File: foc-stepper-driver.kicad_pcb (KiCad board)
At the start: 4 copper layers, 42 x 42 mm, 72 parts, among them CN1 C42391660, CN2 C2839706, CN3 C2839705, CN4 C2839704, J2 TC2030, U1 DRV8962DDWR, U2 TYPE-C 16PLT-H10.0, U3 STM32G431CBT6, U6 AS5047P-ATSM, U7 TPS560430XDBVR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

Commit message: update
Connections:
- U1 pad 45: unconnected-(U1-EP-Pad45) -> GND
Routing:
- net GND: track 61.1 -> 66.2 mm, vias 62 -> 70
- added copper zone on F.Cu, net GND
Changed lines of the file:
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@@
 	(net 79 "/STM32G431CBT6/USBC_CONN_D-")
 	(net 80 "unconnected-(J2-Pad3)")
-	(net 81 "unconnected-(U1-EP-Pad45)")
 	(footprint "Capacitor_SMD:C_0402_1005Metric"
 		(layer "F.Cu")
@@
 			(size 3.9 8)
 			(layers "F.Cu" "F.Mask" "F.Paste")
-			(net 81 "unconnected-(U1-EP-Pad45)")
+			(net 1 "GND")
 			(pinfunction "EP")
-			(pintype "unspecified+no_connect")
+			(pintype "unspecified")
 		)
 		(embedded_fonts no)
@@
 	)
 	(segment
+		(start 145.477834 83.135166)
+		(end 145.05 83.563)
+		(width 0.5)
+		(layer "F.Cu")
+		(net 1)
+	)
+	(segment
 		(start 137.14 77.51)
 		(end 137.15 77.5)
@@
 	)
 	(segment
+		(start 147.460162 83.135166)
+		(end 145.477834 83.135166)
+		(width 0.5)
+		(layer "F.Cu")
+		(net 1)
+	)
+	(segment
 		(start 129.169 77.3)
 		(end 129.92 77.3)
@@
 	)
 	(segment
+		(start 147.458012 83.978553)
+		(end 145.465553 83.978553)
+		(width 0.5)
+		(layer "F.Cu")
+		(net 1)
+	)
+	(segment
 		(start 118.8875 87.860034)
 		(end 120.269966 87.860034)
@@
 	)
 	(segment
+		(start 145.465553 83.978553)
+		(end 145.05 83.563)
+		(width 0.5)
+		(layer "F.Cu")
+		(net 1)
+	)
+	(segment
 		(start 120.269966 87.860034)
 		(end 120.27 87.86)
@@
 	)
 	(via
+		(at 147.38 81.45)
+		(size 0.7)
+		(drill 0.3)
+		(layers "F.Cu" "B.Cu")
+		(free yes)
+		(net 1)
+	)
+	(via
 		(at 131.939635 81.413191)
 		(size 0.4)
@@
 	)
 	(via
+		(at 142.78 83.24)
+		(size 0.4)
+		(drill 0.15)
+		(layers "F.Cu" "B.Cu")
+		(free yes)
+		(net 1)
+	)
+	(via
 		(at 133.705644 92.119356)
 		(size 0.4)
@@
 	)
 	(via
+		(at 147.38 80.5)
+		(size 0.7)
+		(drill 0.3)
+		(layers "F.Cu" "B.Cu")
+		(free yes)
+		(net 1)
+	)
+	(via
 		(at 124.73 68.17)
 		(size 0.4)
@@
 	)
 	(via
+		(at 147.38 86.71)
+		(size 0.7)
+		(drill 0.3)
+		(layers "F.Cu" "B.Cu")
+		(free yes)
+		(net 1)
+	)
+	(via
 		(at 116.43 83.07)
 		(size 0.5)
@@
 	)
 	(via
+		(at 147.38 82.42)
+		(size 0.7)
+		(drill 0.3)
+		(layers "F.Cu" "B.Cu")
+		(free yes)
+		(net 1)
+	)
+	(via
+		(at 147.38 84.79)
+		(size 0.7)
+		(drill 0.3)
+		(layers "F.Cu" "B.Cu")
+		(free yes)
+		(net 1)
+	)
+	(via
 		(at 147.458012 83.978553)
 		(size 0.6)
@@
 	)
 	(via
+		(at 147.38 85.75)
+		(size 0.7)
+		(drill 0.3)
+		(layers "F.Cu" "B.Cu")
+		(free yes)
+		(net 1)
+	)
+	(via
 		(at 129.1 93.62)
 		(size 0.4)
@@
 	)
 	(via
+		(at 142.76 80.7)
+		(size 0.4)
+		(drill 0.15)
+		(layers "F.Cu" "B.Cu")
+		(free yes)
+		(net 1)
+	)
+	(via
 		(at 120.27 87.86)
 		(size 0.4)
@@
 	)
 	(segment
-		(start 135.31 82.45)
-		(end 135.310876 82.449124)
-		(width 0.29)
+		(start 147.525168 83.135166)
+		(end 147.540002 83.15)
+		(width 0.5)
 		(layer "B.Cu")
 		(net 1)
 	)
 	(segment
-		(start 148.21 83.15)
-		(end 148.27 83.09)
-		(width 0.5)
+		(start 135.31 82.45)
+		(end 135.310876 82.449124)
+		(width 0.29)
 		(layer "B.Cu")
 		(net 1)
 	)
 	(segment
-		(start 147.460162 83.135166)
-		(end 147.525168 83.135166)
+		(start 131.233095 80.246902)
+		(end 130.466902 80.246902)
 		(width 0.5)
 		(layer "B.Cu")
@@
 	)
 	(segment
-		(start 147.458012 83.978553)
-		(end 147.501447 83.978553)
+		(start 138.62 89.17)
+		(end 137.63 89.17)
 		(width 0.5)
 		(layer "B.Cu")
@@
 	)
 	(segment
-		(start 131.233095 80.246902)
-		(end 130.466902 80.246902)
+		(start 147.501447 83.978553)
+		(end 147.51 83.97)
 		(width 0.5)
 		(layer "B.Cu")
@@
 	)
 	(segment
-		(start 138.62 89.17)
-		(end 137.63 89.17)
+		(start 147.540002 83.15)
+		(end 148.21 83.15)
 		(width 0.5)
 		(layer "B.Cu")
@@
 	)
 	(segment
-		(start 137.7 92.32)
-		(end 137.67 92.29)
+		(start 147.458012 83.978553)
+		(end 147.501447 83.978553)
 		(width 0.5)
 		(layer "B.Cu")
@@
 	)
 	(segment
-		(start 137.63 89.17)
-		(end 137.62 89.18)
+		(start 148.21 83.15)
+		(end 148.27 83.09)
 		(width 0.5)
 		(layer "B.Cu")
@@
 	)
 	(segment
-		(start 147.501447 83.978553)
-		(end 147.51 83.97)
+		(start 137.7 92.32)
+		(end 137.67 92.29)
 		(width 0.5)
 		(layer "B.Cu")
@@
 	)
 	(segment
-		(start 147.540002 83.15)
-		(end 148.21 83.15)
+		(start 147.51 83.97)
+		(end 148.23 83.97)
 		(width 0.5)
 		(layer "B.Cu")
@@
 	)
 	(segment
-		(start 147.525168 83.135166)
-		(end 147.540002 83.15)
+		(start 137.63 89.17)
+		(end 137.62 89.18)
 		(width 0.5)
 		(layer "B.Cu")
@@
 	)
 	(segment
+		(start 147.460162 83.135166)
+		(end 147.525168 83.135166)
+		(width 0.5)
+		(layer "B.Cu")
+		(net 1)
+	)
+	(segment
 		(start 130.466902 80.246902)
 		(end 130.46 80.24)
@@
 	)
 	(segment
-		(start 147.51 83.97)
-		(end 148.23 83.97)
-		(width 0.5)
-		(layer "B.Cu")
-		(net 1)
-	)
-	(segment
 		(start 132.42 90.279774)
 		(end 131.594774 91.105)
@@
 			)
 		)
+	)
+	(zone
+		(net 1)
+		(net_name "GND")
+		(layer "F.Cu")
+		(hatch edge 0.5)
+		(priority 35)
+		(connect_pads yes
+			(clearance 0.3)
+		)
+		(min_thickness 0.25)
+		(filled_areas_thickness no)
+		(fill yes
+			(thermal_gap 0.5)
+			(thermal_bridge_width 0.5)
+		)
+		(polygon
+			(pts
+				(xy 142.96 79.4) (xy 142.96 87.71) (xy 147.16 87.71) (xy 147.83 87.04) (xy 147.83 80.17) (xy 147.06 79.4)
+			)
+		)

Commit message: update
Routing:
- net +24V: track 11.1 -> 22.1 mm, vias 2 -> 10
- net GND: track 66.2 -> 66.6 mm, vias 70 -> 68

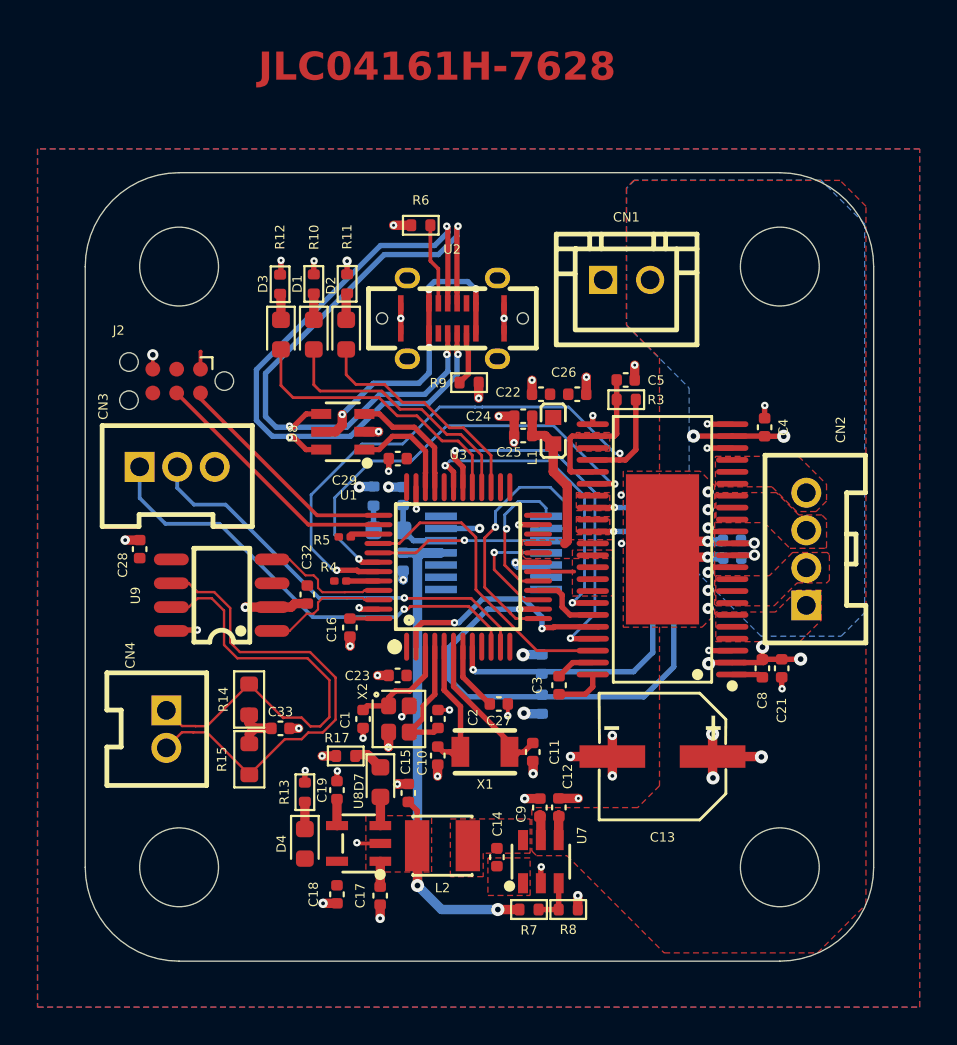
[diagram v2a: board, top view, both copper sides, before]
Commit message: update trace width
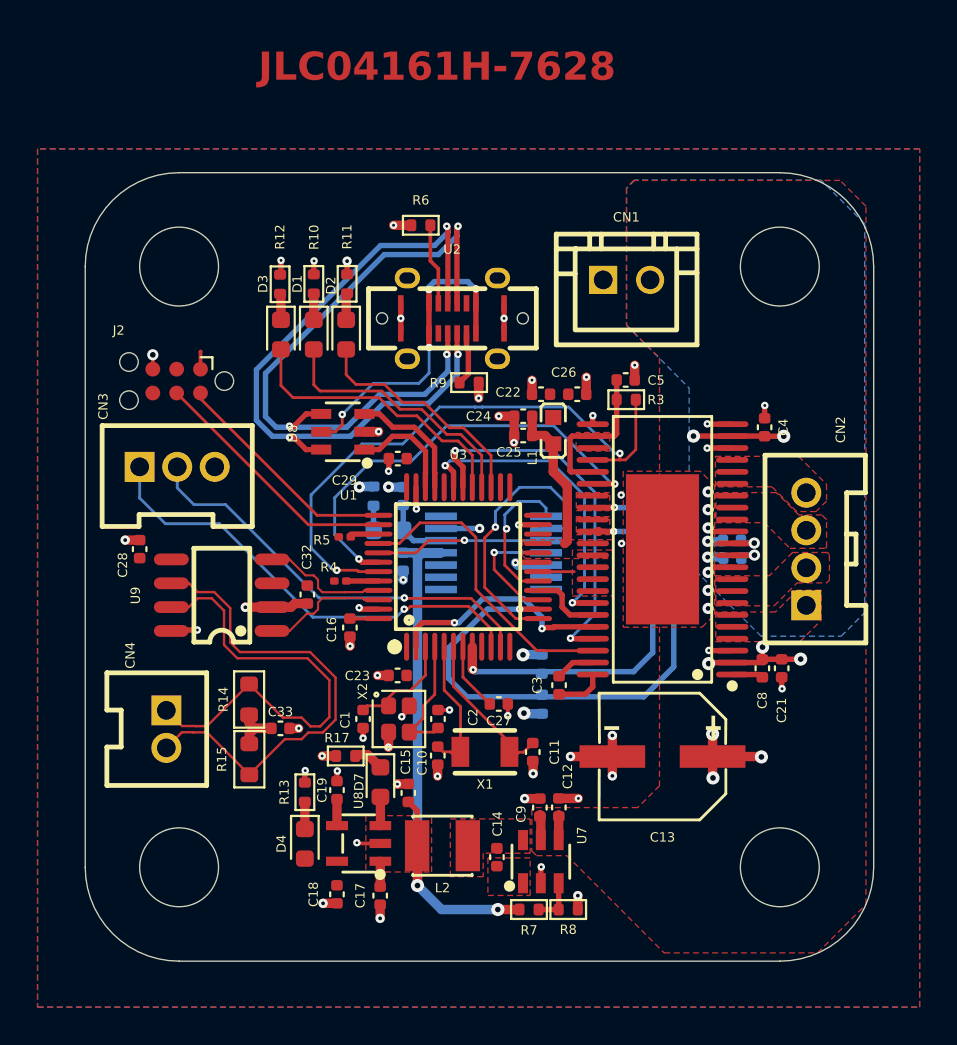
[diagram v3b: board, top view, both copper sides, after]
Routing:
- net GND: track 66.6 -> 62.6 mm

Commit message: update
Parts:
- R14, R15: value 60 -> 60.4; footprint PCM_Resistor_SMD_AKL:R_0603_1608Metric -> PCM_Resistor_SMD_AKL:R_0402_1005Metric
- moved R17 9.13 mm to (130.6, 103.4), turned to 0 degrees
- moved R13 7.08 mm to (124.4, 103.4), turned to 180 degrees
- moved D7 6.73 mm to (128.6, 102.5), turned to 90 degrees
- moved C32 5.68 mm to (121.6, 82.6), turned to 180 degrees
- moved C18 3.79 mm to (124.9, 99.4), turned to -90 degrees
- moved C22 3.65 mm to (137.5, 78.8)
- moved D4 3.33 mm to (126.2, 102.6), turned to 90 degrees
- moved C17 2.56 mm to (130.1, 99.5), turned to -90 degrees
- moved C15 1.75 mm to (130.1, 97.5)
- moved U8 1.44 mm to (127.5, 98.9)
- moved C19 1.42 mm to (126.3, 96.2)
- moved C23 1.19 mm to (129.8, 90.3)
- moved C16 1.11 mm to (128.4, 88.8)
- moved J2 1.05 mm to (119.2, 73.5)
- moved CN3 0.92 mm to (119.2, 78.2)
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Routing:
- net +3.3V: track 2.48 -> 30.8 mm, vias 0 -> 12
- net /STM32G431CBT6/USBC_CONN_D-: track 35.5 -> 15.8 mm, vias 3 -> 2
- net /STM32G431CBT6/USBC_CONN_D+: track 37.1 -> 19.8 mm
- net +24V: track 22.1 -> 29.8 mm
- net +5V: track 34.4 -> 31.1 mm
- net /DRV8962DDWR/DRV8962_IPROPI1: track 20.2 -> 17.1 mm
- net /DRV8962DDWR/DRV8962_IPROPI3: track 31.9 -> 29.8 mm
- net /DRV8962DDWR/DRV8962_nFAULT: track 31.9 -> 33.9 mm
- net GND: track 62.6 -> 61.1 mm, vias 68 -> 54
- net Net-(C33-Pad1): track 3.64 -> 2.46 mm
- net /STM32G431CBT6/STM32_SWCLK: track 13.7 -> 14.8 mm
- net Net-(D8-Pad5): track 17.1 -> 18.1 mm
- net /STM32G431CBT6/STM32_SWDIO: track 12.4 -> 13.2 mm
- net /STM32G431CBT6/STM32_USART_TX: track 24.7 -> 25.4 mm
- net /AS5047P/AS5047P_SPI_CSn: track 7.96 -> 8.61 mm
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- added copper zone on In2.Cu, net +3.3V
- removed copper zone on In2.Cu, net GND

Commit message: update
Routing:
- net GND: track 61.1 -> 62.8 mm, vias 54 -> 56
- net /DRV8962DDWR/DRV8962_nFAULT: track 33.9 -> 34.6 mm

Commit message: update
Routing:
- net GND: track 62.8 -> 63.1 mm, vias 56 -> 59

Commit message: update
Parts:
- moved C30 0.28 mm to (131.0, 84.2)
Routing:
- net /DRV8962DDWR/DRV8962_EN: track 1.93 -> 0.00 mm
- net +3.3V: track 30.8 -> 29.6 mm
- removed copper zone on F.Cu, net +3.3V
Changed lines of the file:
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@@
 	(footprint "Capacitor_SMD:C_0402_1005Metric"
 		(layer "B.Cu")
-		(at 131.233095 84.225 -90)
+		(at 130.96 84.19 -90)
 		(descr "Capacitor SMD 0402 (1005 Metric), square (rectangular) end terminal, IPC-7351 nominal, (Body size source: IPC-SM-782 page 76, https://www.pcb-3d.com/wordpress/wp-content/uploads/ipc-sm-782a_amendment_1_and_2.pdf), generated with kicad-footprint-generator")
 		(tags "capacitor")
@@
 	)
 	(segment
-		(start 147.592678 88.9605)
-		(end 147.532452 88.900274)
-		(width 0.29)
-		(layer "F.Cu")
-		(net 1)
-	)
-	(segment
 		(start 137.15 77.34)
 		(end 136.485 77.34)
@@
 	)
 	(segment
+		(start 147.720489 88.9605)
+		(end 148.7645 88.9605)
+		(width 0.29)
+		(layer "F.Cu")
+		(net 1)
+	)
+	(segment
 		(start 128.47 90.28)
 		(end 128.46 90.27)
@@
 	)
 	(segment
-		(start 148.7645 88.9605)
-		(end 147.592678 88.9605)
-		(width 0.29)
-		(layer "F.Cu")
-		(net 1)
-	)
-	(segment
 		(start 139.53 96.83)
 		(end 140.57 96.83)
@@
 		(net 1)
 	)
+	(segment
+		(start 147.679439 88.91945)
+		(end 147.720489 88.9605)
+		(width 0.29)
+		(layer "F.Cu")
+		(net 1)
+	)
 	(via
 		(at 132.32 103.35)
@@
 	)
 	(via
-		(at 147.43 78.17)
+		(at 131.247313 85.40185)
 		(size 0.6)
 		(drill 0.3)
@@
 	)
 	(via
-		(at 141.34 76.44)
+		(at 147.43 78.17)
 		(size 0.6)
 		(drill 0.3)
@@
 	)
 	(via
-		(at 137.71 96.84)
+		(at 141.34 76.44)
 		(size 0.6)
 		(drill 0.3)
@@
 	)
 	(via
-		(at 131.24 85.19)
+		(at 137.71 96.84)
 		(size 0.6)
 		(drill 0.3)
@@
 	)
 	(via
-		(at 147.532452 88.900274)
+		(at 147.679439 88.91945)
 		(size 0.6)
 		(drill 0.3)
@@
 	)
 	(segment
-		(start 148.27 83.09)
-		(end 147.4 83.09)
+		(start 131.233095 85.387632)
+		(end 131.247313 85.40185)
 		(width 0.29)
 		(layer "B.Cu")
@@
 	)
 	(segment
-		(start 131.233095 80.246902)
-		(end 130.466902 80.246902)
-		(width 0.5)
+		(start 148.27 83.09)
+		(end 147.4 83.09)
+		(width 0.29)
 		(layer "B.Cu")
 		(net 1)
 	)
 	(segment
-		(start 131.233095 85.183095)
-		(end 131.24 85.19)
+		(start 131.233095 80.246902)
+		(end 130.466902 80.246902)
 		(width 0.5)
 		(layer "B.Cu")
@@
 	)
 	(segment
+		(start 131.233095 84.943095)
+		(end 131.233095 85.387632)
+		(width 0.29)
+		(layer "B.Cu")
+		(net 1)
+	)
+	(segment
 		(start 138.85 84.4)
 		(end 137.345 84.4)
@@
 	)
 	(segment
-		(start 131.233095 84.705)
-		(end 131.233095 85.183095)
-		(width 0.5)
+		(start 130.96 84.67)
+		(end 131.233095 84.943095)
+		(width 0.29)
 		(layer "B.Cu")
 		(net 1)
@@
 	)
 	(segment
-		(start 132.8 102.75)
-		(end 136.28 102.75)
+		(start 133.25 83.75)
+		(end 131.238095 83.75)
 		(width 0.5)
 		(layer "B.Cu")
@@
 	)
 	(segment
-		(start 132 101.47)
-		(end 132 83.99)
+		(start 132.8 102.75)
+		(end 136.28 102.75)
 		(width 0.5)
 		(layer "B.Cu")
@@
 	)
 	(segment
-		(start 131.238095 83.75)
-		(end 131.233095 83.745)
+		(start 131.198095 83.71)
+		(end 130.96 83.71)
 		(width 0.5)
 		(layer "B.Cu")
@@
 	)
 	(segment
-		(start 133.25 83.75)
-		(end 131.238095 83.75)
+		(start 132 101.47)
+		(end 132 83.99)
 		(width 0.5)
 		(layer "B.Cu")
@@
 	)
 	(segment
+		(start 131.238095 83.75)
+		(end 131.198095 83.71)
+		(width 0.5)
+		(layer "B.Cu")
+		(net 11)
+	)
+	(segment
 		(start 120.44 73.09)
 		(end 120.425 73.075)
@@
 	)
 	(segment
-		(start 140.03 74.355)
-		(end 140.025 74.35)
-		(width 0.29)
-		(layer "F.Cu")
-		(net 12)
-	)
-	(segment
 		(start 137.96 78.15)
 		(end 137.95 78.14)
@@
 	)
 	(segment
-		(start 139.06 75.3)
-		(end 139.06 74.335)
-		(width 0.29)
-		(layer "F.Cu")
-		(net 12)
-	)
-	(segment
 		(start 117.270034 84.100034)
 		(end 117.2 84.03)
@@
 	)
 	(segment
+		(start 140.03 75.3)
+		(end 140.03 74.44)
+		(width 0.5)
+		(layer "F.Cu")
+		(net 12)
+	)
+	(segment
 		(start 122.055 82.575)
 		(end 123 82.575)
@@
 	)
 	(segment
-		(start 139.06 75.3)
-		(end 140.03 75.3)
+		(start 127.083805 82.9)
+		(end 127.074821 82.891016)
+		(width 0.5)
+		(layer "F.Cu")
+		(net 12)
+	)
+	(segment
+		(start 137.96 78.78)
+		(end 138.42 79.24)
 		(width 0.29)
 		(layer "F.Cu")
@@
 	)
 	(segment
-		(start 127.083805 82.9)
-		(end 127.074821 82.891016)
+		(start 139.23 76.54)
+		(end 139.23 75.675)
 		(width 0.5)
 		(layer "F.Cu")
@@
 	)
 	(segment
-		(start 120.44 71.76)
-		(end 120.45 71.75)
-		(width 0.5)
+		(start 138.42 79.24)
+		(end 138.42 81.75)
+		(width 0.29)
 		(layer "F.Cu")
 		(net 12)
 	)
 	(segment
-		(start 139.06 74.335)
-		(end 139.05 74.325)
-		(width 0.29)
+		(start 120.44 71.76)
+		(end 120.45 71.75)
+		(width 0.5)
 		(layer "F.Cu")
 		(net 12)
 	)
 	(segment
-		(start 138.08 78.78)
-		(end 137.96 78.78)
-		(width 0.15)
+		(start 139.23 75.675)
+		(end 139.21 75.655)
+		(width 0.5)
 		(layer "F.Cu")
 		(net 12)
 	)
 	(segment
-		(start 138.42 81.75)
-		(end 138.42 79.12)
-		(width 0.15)
+		(start 140.03 74.44)
+		(end 140.01 74.42)
+		(width 0.5)
 		(layer "F.Cu")
 		(net 12)
@@
 	)
 	(segment
-		(start 138.42 79.12)
-		(end 138.08 78.78)
-		(width 0.15)
-		(layer "F.Cu")
-		(net 12)
-	)
-	(segment
 		(start 126.301 99.89975)
 		(end 124.91975 99.89975)
@@
 	)
 	(segment
-		(start 140.03 75.3)
-		(end 140.03 74.355)
-		(width 0.29)
-		(layer "F.Cu")
-		(net 12)
-	)
-	(segment
 		(start 124.91975 99.89975)
 		(end 124.9 99.88)
@@
 	)
 	(via
-		(at 140.025 74.35)
-		(size 0.6)
-		(drill 0.3)
-		(layers "F.Cu" "B.Cu")
-		(net 12)
-	)
-	(via
 		(at 120.45 71.75)
 		(size 0.6)
@@
 	)
 	(via
-		(at 139.05 74.325)
+		(at 117.2 84.925)
 		(size 0.6)
 		(drill 0.3)
@@
 	)
 	(via
-		(at 117.2 84.925)
+		(at 140.01 74.42)
 		(size 0.6)
 		(drill 0.3)
@@
 	)
 	(via
+		(at 139.21 75.655)
+		(size 0.6)
+		(drill 0.3)
+		(layers "F.Cu" "B.Cu")
+		(net 12)
+	)
+	(via
 		(at 123.85 99.88)
 		(size 0.6)
@@
 	)
 	(segment
-		(start 138.42 84.75)
-		(end 140.35 84.75)
-		(width 0.15)
-		(layer "F.Cu")
-		(net 51)
-	)
-	(segment
 		(start 140.054042 87.0555)
 		(end 141.3355 87.0555)
@@
 	)
 	(zone
-		(net 7)
-		(net_name "/DRV8962DDWR/DRV8962_DVDD")
+		(net 51)
+		(net_name "/DRV8962DDWR/DRV8962_EN")
 		(layer "F.Cu")
 		(hatch edge 0.5)
-		(priority 30)
+		(priority 25)
 		(connect_pads yes
-			(clearance 0.25)
+			(clearance 0)
 		)
 		(min_thickness 0.25)
@@
 			(thermal_gap 0.5)
 			(thermal_bridge_width 0.5)
-			(island_removal_mode 1)
-			(island_area_min 10)
 		)
 		(polygon
 			(pts
-				(xy 140.45 78.33) (xy 142.24 78.33) (xy 142.24 77.36) (xy 142.22 77.34) (xy 140.45 77.34)
+				(xy 137.76 84.55) (xy 137.65 84.66) (xy 137.65 84.85) (xy 137.76 84.96) (xy 139.3 84.96) (xy 140.33 85.99)
+				(xy 142.17 85.99) (xy 142.22 85.94) (xy 142.22 83.74) (xy 142.18 83.7) (xy 140.28 83.7) (xy 139.43 84.55)
 			)
 		)
 	)
 	(zone
-		(net 12)
-		(net_name "+3.3V")
+		(net 7)
+		(net_name "/DRV8962DDWR/DRV8962_DVDD")
 		(layer "F.Cu")
 		(hatch edge 0.5)
-		(priority 1)
-		(connect_pads thru_hole_only
-			(clearance 0.15)
+		(priority 30)
+		(connect_pads yes
+			(clearance 0.25)
 		)
-		(min_thickness 0.15)
+		(min_thickness 0.25)
 		(filled_areas_thickness no)
 		(fill yes
-			(thermal_gap 0.4)
-			(thermal_bridge_width 0.4)
+			(thermal_gap 0.5)
+			(thermal_bridge_width 0.5)
+			(island_removal_mode 1)
+			(island_area_min 10)
 		)
 		(polygon
 			(pts
-				(xy 138.725 77.1) (xy 139.725 77.1) (xy 140 76.825) (xy 140 76.1) (xy 140.375 75.725) (xy 140.5 75.725)
-				(xy 140.51 75.715) (xy 140.51 74.825) (xy 138.725 74.825)
+				(xy 140.45 78.33) (xy 142.24 78.33) (xy 142.24 77.36) (xy 142.22 77.34) (xy 140.45 77.34)
 			)
 		)
@@
 			)
 		)
-	)
-	(zone
-		(net 51)
-		(net_name "/DRV8962DDWR/DRV8962_EN")
-		(layer "F.Cu")
-		(hatch edge 0.5)
-		(priority 8)
-		(connect_pads yes
-			(clearance 0)
-		)
-		(min_thickness 0.25)
-		(filled_areas_thickness no)
-		(fill yes
-			(thermal_gap 0.5)
-			(thermal_bridge_width 0.5)
-		)
-		(polygon
-			(pts
-				(xy 140.25 86.05) (xy 142.35 86.05) (xy 142.4 86) (xy 142.4 83.65) (xy 142.35 83.6) (xy 140.25 83.6)
-			)
-		)
